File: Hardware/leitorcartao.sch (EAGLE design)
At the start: 168 parts, among them IC1 TL084, IC2 TL084, Q1 BSH103, Q2 BC847ASMD, Q3 BC857ALT1SMD, Q4 BC847ALT1SMD, Q5 BC847ALT1SMD, Q6 BC847ALT1SMD, Q7 BC847ALT1SMD, U1 SAMD20E14A-AUT, U3 TLV1117-50CDCYR, U4 MFRC52202HN1, U5 LP2985-33DBVR, X1 ANTENA 125kHz, X2 MIFARE ANTENA

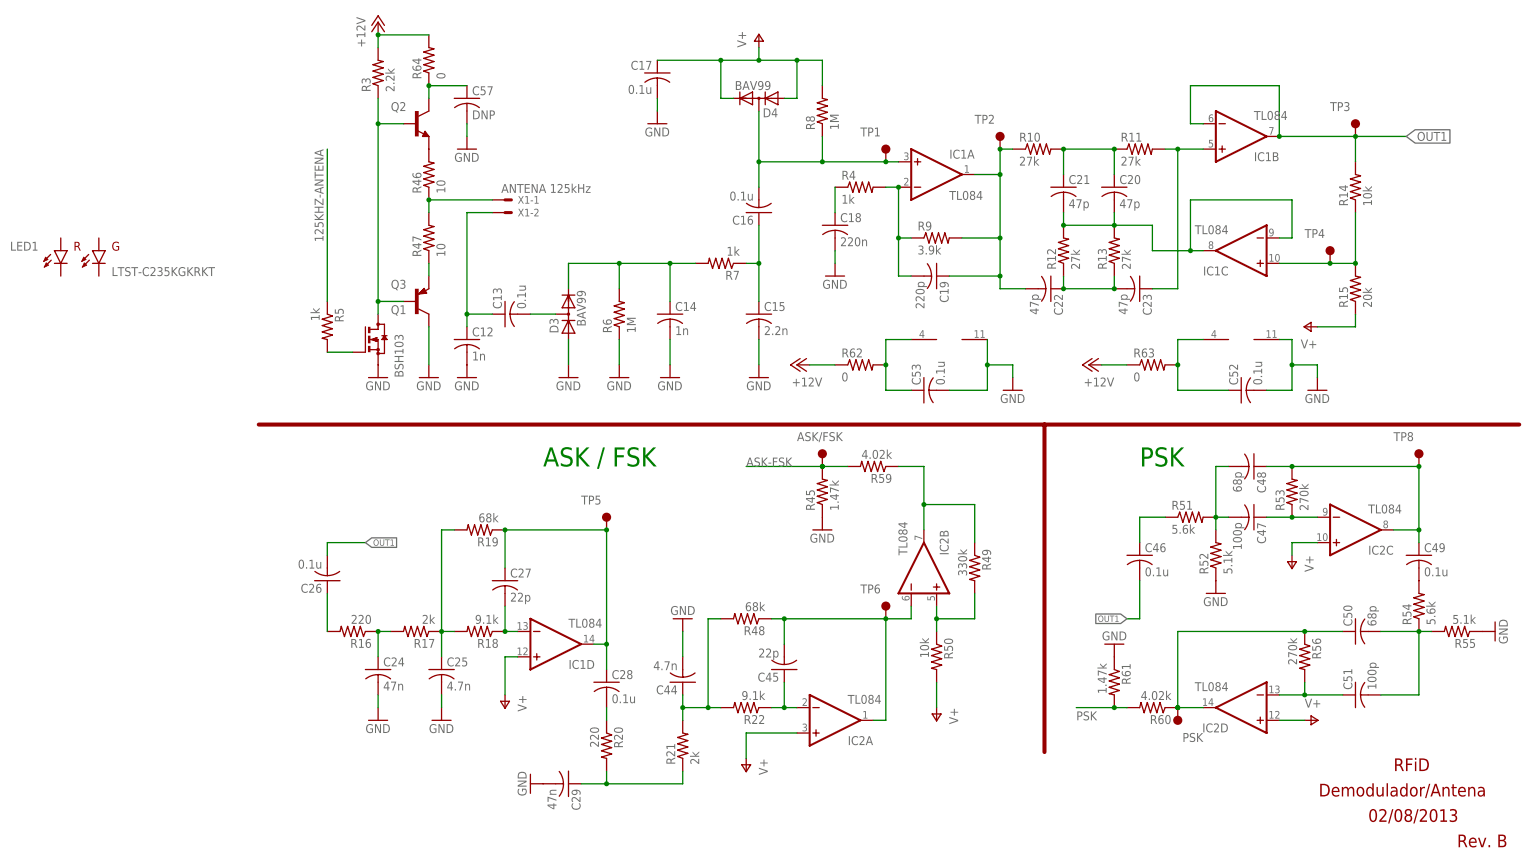
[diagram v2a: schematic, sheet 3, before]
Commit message: Alterações  do valor dos divisores resisitivos.
Coloção de 4 furos de fontagem M2.
Troca do LED PLCC4 por um mais barato.
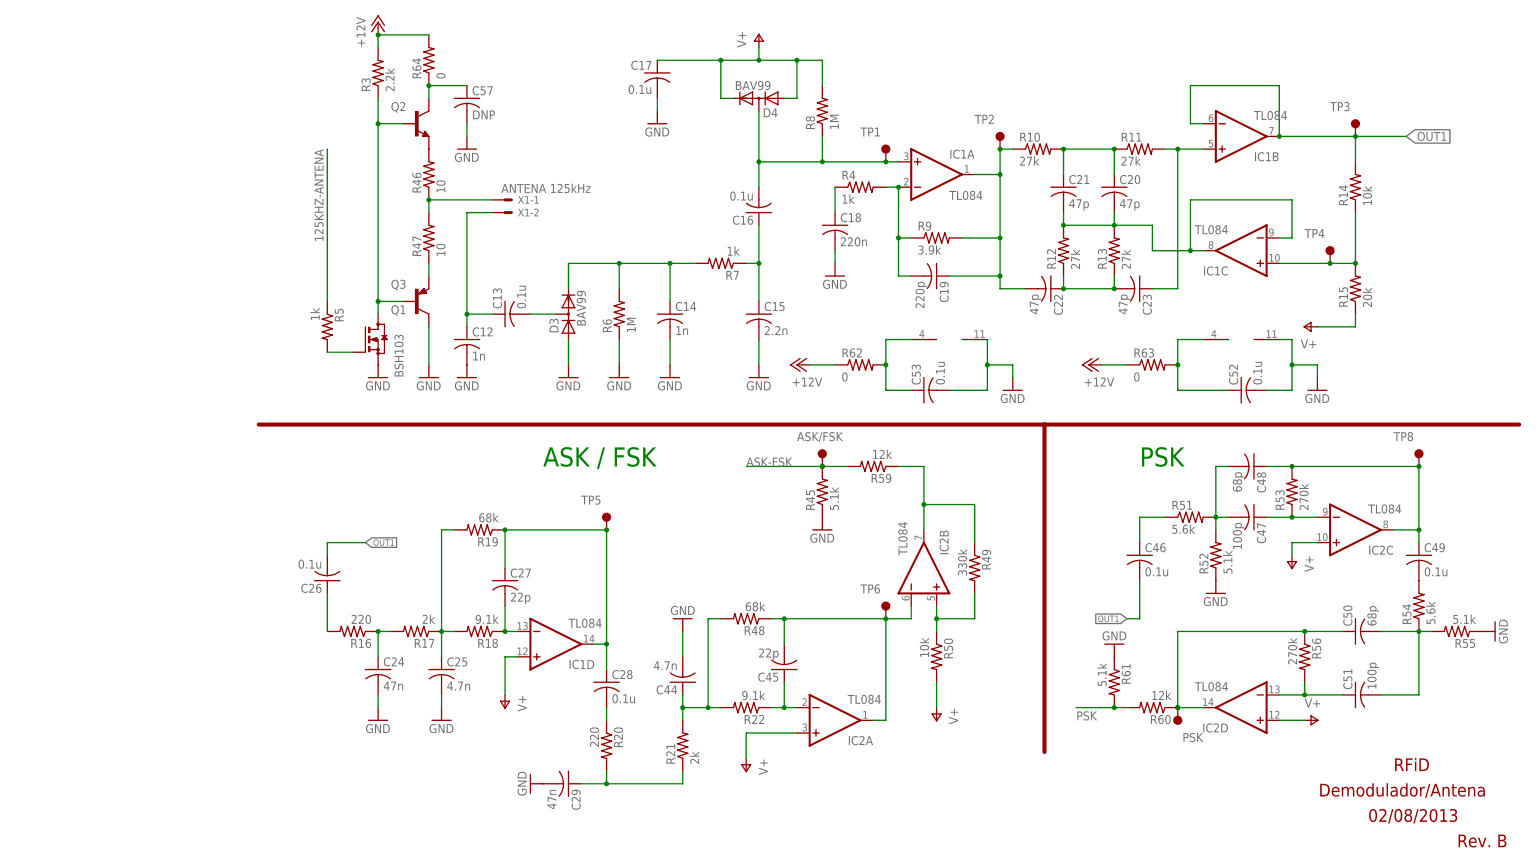
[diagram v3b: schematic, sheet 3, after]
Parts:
- removed LED2: SMP4-SBC, RFiD:SMP4-SBC
- R45, R61: value 1.47k -> 5.1k
- R59, R60: value 4.02k -> 12k
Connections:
- net LED-GREEN-CTRL: now also LED1.1; no longer LED2.1
- net LED-RED-CTRL: now also LED1.4; no longer LED2.3
- net N$52: now also LED1.3; no longer LED2.4
- net N$53: now also LED1.2; no longer LED2.2
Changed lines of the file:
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@@
 <part name="SWD" library="pinhead" deviceset="PINHD-1X5" device=""/>
 <part name="R23" library="RFiD" deviceset="R-US_" device="R0402" value="10k"/>
-<part name="LED2" library="RFiD" deviceset="SMP4-SBC" device=""/>
 <part name="R46" library="RFiD" deviceset="R-US_" device="R0603" value="10">
 <attribute name="CUSTOMER_PN" value="R/39/5%/04"/>
@@
 <part name="P+7" library="supply1" deviceset="V+" device=""/>
 <part name="+3V17" library="supply1" deviceset="+3V3" device=""/>
-<part name="R45" library="RFiD" deviceset="R-US_" device="R0402" value="1.47k">
+<part name="R45" library="RFiD" deviceset="R-US_" device="R0402" value="5.1k">
 <attribute name="CUSTOMER_PN" value="R/1k/5%/04"/>
 </part>
-<part name="R59" library="RFiD" deviceset="R-US_" device="R0402" value="4.02k">
+<part name="R59" library="RFiD" deviceset="R-US_" device="R0402" value="12k">
 <attribute name="CUSTOMER_PN" value="R/1k/5%/04"/>
 </part>
 <part name="GND53" library="supply1" deviceset="GND" device=""/>
-<part name="R60" library="RFiD" deviceset="R-US_" device="R0402" value="4.02k">
+<part name="R60" library="RFiD" deviceset="R-US_" device="R0402" value="12k">
 <attribute name="CUSTOMER_PN" value="R/1k/5%/04"/>
 </part>
-<part name="R61" library="RFiD" deviceset="R-US_" device="R0402" value="1.47k">
+<part name="R61" library="RFiD" deviceset="R-US_" device="R0402" value="5.1k">
 <attribute name="CUSTOMER_PN" value="R/1k/5%/04"/>
 </part>
@@
 </instance>
 <instance part="GND59" gate="1" x="45.72" y="144.78"/>
-<instance part="LED1" gate="G$1" x="-30.48" y="121.92"/>
 </instances>
 <busses>
@@
 <instance part="+3V18" gate="G$1" x="198.12" y="162.56"/>
 <instance part="+3V19" gate="G$1" x="198.12" y="132.08"/>
-<instance part="LED2" gate="G$1" x="106.68" y="129.54" smashed="yes" rot="R90">
-<attribute name="NAME" x="111.76" y="139.7" size="1.778" layer="95" rot="R180"/>
-<attribute name="VALUE" x="111.76" y="121.92" size="1.778" layer="96" rot="R180"/>
-</instance>
 <instance part="SJ?1" gate="G$1" x="35.56" y="154.94" rot="R180"/>
 <instance part="P+16" gate="1" x="48.26" y="162.56"/>
+<instance part="LED1" gate="G$1" x="106.68" y="132.08" rot="R90"/>
 </instances>
 <busses>
@@
 <pinref part="R41" gate="G$1" pin="2"/>
 <wire x1="88.9" y1="127" x2="101.6" y2="127" width="0.1524" layer="91"/>
-<pinref part="LED2" gate="G$1" pin="4"/>
+<pinref part="LED1" gate="G$1" pin="3"/>
 </segment>
 </net>
@@
 <pinref part="R42" gate="G$1" pin="1"/>
 <wire x1="93.98" y1="134.62" x2="101.6" y2="134.62" width="0.1524" layer="91"/>
-<pinref part="LED2" gate="G$1" pin="2"/>
+<pinref part="LED1" gate="G$1" pin="2"/>
 </segment>
 </net>
@@
 <wire x1="109.22" y1="134.62" x2="137.16" y2="134.62" width="0.1524" layer="91"/>
 <label x="114.3" y="134.62" size="1.778" layer="95"/>
-<pinref part="LED2" gate="G$1" pin="1"/>
+<pinref part="LED1" gate="G$1" pin="1"/>
 </segment>
 </net>
@@
 <wire x1="137.16" y1="127" x2="109.22" y2="127" width="0.1524" layer="91"/>
 <label x="116.84" y="127" size="1.778" layer="95"/>
-<pinref part="LED2" gate="G$1" pin="3"/>
-</segment>
-</net>
+<pinref part="LED1" gate="G$1" pin="4"/>
+</segment>
+</net>

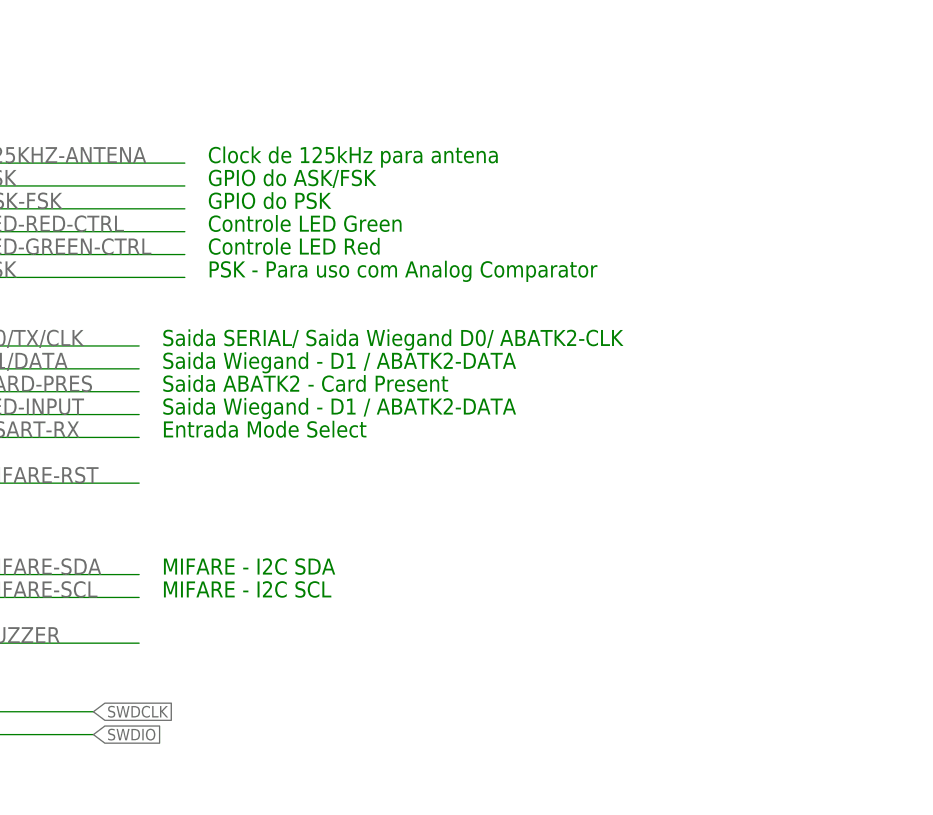
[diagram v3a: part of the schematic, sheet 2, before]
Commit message: Criados polígonos de alimentação.
Correção dos comentários nas páginas do esquema elétrico.
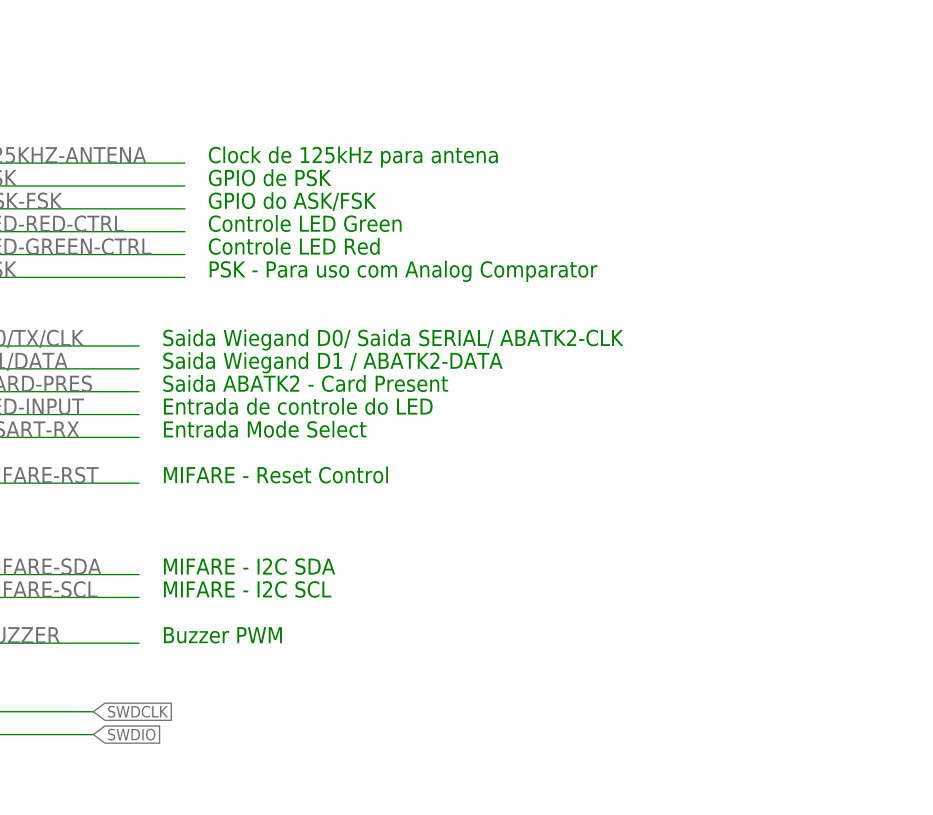
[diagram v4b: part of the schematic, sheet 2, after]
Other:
- note added: "Buzzer PWM"
- note added: "Entrada de controle do LED"
- note added: "GPIO de PSK"
- note added: "MIFARE - Reset Control"
- note added: "Saida Wiegand D0/ Saida SERIAL/ ABATK2-CLK"
- note added: "Saida Wiegand D1 / ABATK2-DATA"
- note removed: "GPIO do PSK"
- note removed: "Saida SERIAL/ Saida Wiegand D0/ ABATK2-CLK"
- note removed: "Saida Wiegand - D1 / ABATK2-DATA"
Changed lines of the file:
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@@
 <text x="193.04" y="81.28" size="3.81" layer="91" ratio="10">Debug/Prog</text>
 <text x="190.5" y="119.38" size="1.4224" layer="91" rot="R180">16V</text>
-<text x="66.04" y="124.46" size="1.778" layer="91">GPIO do ASK/FSK</text>
+<text x="66.04" y="124.46" size="1.778" layer="91">GPIO de PSK</text>
 <text x="60.96" y="96.52" size="1.778" layer="91">Entrada Mode Select</text>
 <text x="66.04" y="127" size="1.778" layer="91">Clock de 125kHz para antena</text>
-<text x="60.96" y="104.14" size="1.778" layer="91">Saida Wiegand - D1 / ABATK2-DATA</text>
-<text x="66.04" y="121.92" size="1.778" layer="91">GPIO do PSK</text>
+<text x="60.96" y="104.14" size="1.778" layer="91">Saida Wiegand D1 / ABATK2-DATA</text>
+<text x="66.04" y="121.92" size="1.778" layer="91">GPIO do ASK/FSK</text>
 <text x="66.04" y="116.84" size="1.778" layer="91">Controle LED Red</text>
 <text x="66.04" y="119.38" size="1.778" layer="91">Controle LED Green</text>
-<text x="60.96" y="106.68" size="1.778" layer="91">Saida SERIAL/ Saida Wiegand D0/ ABATK2-CLK</text>
+<text x="60.96" y="106.68" size="1.778" layer="91">Saida Wiegand D0/ Saida SERIAL/ ABATK2-CLK</text>
 <text x="60.96" y="78.74" size="1.778" layer="91">MIFARE - I2C SCL</text>
 <text x="60.96" y="81.28" size="1.778" layer="91">MIFARE - I2C SDA</text>
 <text x="60.96" y="101.6" size="1.778" layer="91">Saida ABATK2 - Card Present</text>
-<text x="60.96" y="99.06" size="1.778" layer="91">Saida Wiegand - D1 / ABATK2-DATA</text>
+<text x="60.96" y="99.06" size="1.778" layer="91">Entrada de controle do LED</text>
 <text x="243.84" y="5.08" size="2.54" layer="94">Rev. B</text>
 <text x="66.04" y="114.3" size="1.778" layer="91">PSK - Para uso com Analog Comparator</text>
+<text x="60.96" y="73.66" size="1.778" layer="91">Buzzer PWM</text>
+<text x="60.96" y="91.44" size="1.778" layer="91">MIFARE - Reset Control</text>
 </plain>
 <instances>

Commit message: Início da versão 3.0
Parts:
- removed C19: 220p, RFiD:C-USC0402
- removed D4: BAV99, RFiD:BAV99
- removed Q2: BC847ASMD, RFiD:BC847ASMD
- removed Q3: BC857ALT1SMD, RFiD:BC857ALT1SMD
- removed R14, R50: 10k, RFiD:R-US_R0402
- removed R15: 20k, RFiD:R-US_R0402
- removed R49: 330k, RFiD:R-US_R0402
- removed TP1, TP2, TP3, TP4: TESTPOINT, RFiD:TESTPOINT
- added Q8: MMBT4403, RFiD:MMBT4403
- added Q9: MMBT4401, RFiD:MMBT4401
- C12: device RFiD:C-USC0603 -> RFiD:C-USC1812; CUSTOMER_PN C/1n/100V/C04 -> (none)
- C13: value 0.1u -> 1n; device RFiD:C-USC0603 -> RFiD:C-USC1206; CUSTOMER_PN C/0.1u/50V/C04 -> (none)
- C14: device RFiD:C-USC0603 -> RFiD:C-USC1206
- C15: value 2.2n -> 220n; device RFiD:C-USC0603 -> RFiD:C-USC1206; CUSTOMER_PN C/2.2n/100V/D04 -> (none)
- C16: value 0.1u -> (none); device RFiD:C-USC0603 -> RFiD:C-USC0402; CUSTOMER_PN C/0.1u/50V/C04 -> C/2.2n/100V/D04
- C18: value 220n -> (none)
- D3: value BAV99 -> US1J-13-F; device RFiD:BAV99 -> RFiD:US1J-13-F
- Q1: value BSH103 -> DMN3404; device RFiD:BSS123 -> RFiD:DMN3404; CUSTOMER_PN Q/BSH103 -> (none)
- R4: value 1k -> (none)
- R6: device RFiD:R-US_R0603 -> RFiD:R-US_R1206
- R7: value 1k -> (none); device RFiD:R-US_R0603 -> RFiD:R-US_R0402; CUSTOMER_PN R/1k/5%/04 -> R/1M/5%/04
- R8: value 1M -> 100k
- R9: value 3.9k -> (none)
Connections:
- removed net N$17: C19.1, C22.2, IC1A.OUT, R10.1, R9.2, TP2.1
- removed net N$21: C20.2, C21.2, IC1C.-IN, IC1C.OUT, R12.2, R13.2
- removed net N$26: IC1C.+IN, R14.1, R15.2, TP4.1
- removed net N$59: Q2.E, R46.2
- removed net N$65: C45.2, IC2A.OUT, IC2B.-IN, R48.1, TP6.1
- removed net N$66: IC2B.+IN, R49.2, R50.1
- removed net OUT1: C26.2, C46.2, IC1B.-IN, IC1B.OUT, R14.2, TP3.1
- new net ASK: C18.1, C22.2, C26.2, IC1B.OUT, R10.1, R9.1
- new net FSK/PSK: IC2A.OUT
- net GND: now also C13.2, C16.2, Q8.C; no longer C15.2, C18.2, D3.1, Q3.C
- net N$10: now also IC1A.-IN, IC1A.OUT; no longer C18.1
- net N$12: now also C16.1, R4.2, R7.1, R9.2; no longer C13.2, D3.3
- net N$13: now also C15.1, D3.K; no longer D3.2, R7.2
- net N$14: now also C15.2, IC1A.+IN, R8.1; no longer C15.1, C16.1, R7.1
- net N$15: now also C18.2, IC1B.-IN, R7.2; no longer C19.2, IC1A.-IN, R4.2, R9.1
- net N$16: now also Q9.E, R46.2; no longer C16.2, D4.3, IC1A.+IN, R8.1, TP1.1
- net N$23: now also IC2A.+IN; no longer IC1B.+IN
- net N$27: now also IC1C.+IN; no longer IC1D.-IN
- net N$28: now also IC1C.OUT; no longer IC1D.OUT
- net N$40: now also IC2C.OUT; no longer IC2D.OUT
- net N$48: now also Q9.C; no longer Q2.C
- net N$60: now also Q8.E; no longer Q3.E
- net N$64: now also IC1D.+IN; no longer IC2A.-IN
- net N$7: now also Q8.B, Q9.B; no longer Q2.B, Q3.B
- net N$71: now also IC2B.OUT; no longer IC2C.OUT
- net N$72: now also IC2B.+IN; no longer IC2C.-IN
- net N$75: now also IC2C.-IN; no longer IC2D.-IN
- net N$9: now also D3.A
- net N$90: now also C45.2, IC1D.OUT, R48.1, TP6.1; no longer IC2B.OUT, R49.1
- net V+: now also C20.2, C21.2, IC1B.+IN, IC1C.-IN, IC1D.-IN, IC2A.-IN, IC2B.-IN, R12.2, R13.2; no longer D4.1, D4.2, IC1D.+IN, IC2A.+IN, IC2D.+IN, R15.1, R50.2
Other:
- note added: "ASK/FSK/PSK"
- note added: "FSK/PSK only"
- note added: "Low Pass Filter Q=0.5 / Fc=?"
- note added: "Twin-T Notch Filter Fc=125.417kHz"
- note added: "Voltage Follower"
- moved on the sheet: ASK/FSK, C12, C13, C14, C15, C16, C17, C18, C20, C21, C22, C23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
